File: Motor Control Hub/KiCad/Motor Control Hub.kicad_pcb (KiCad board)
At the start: 2 copper layers, 65 x 41 mm, 8 parts, among them J2 GPIO, J3 Voltage Supply, J4 Motor Controllers

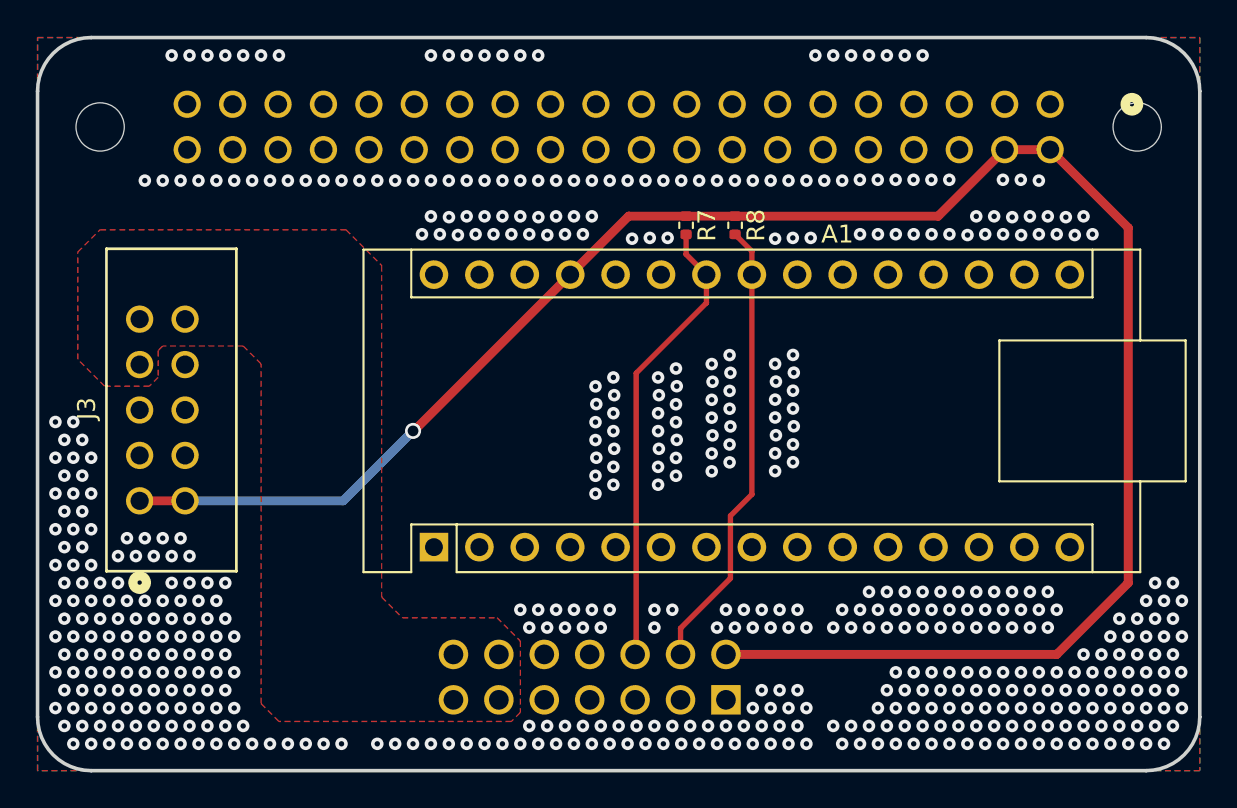
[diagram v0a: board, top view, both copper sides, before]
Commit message: added encoders, slightly adjusted copper tracks
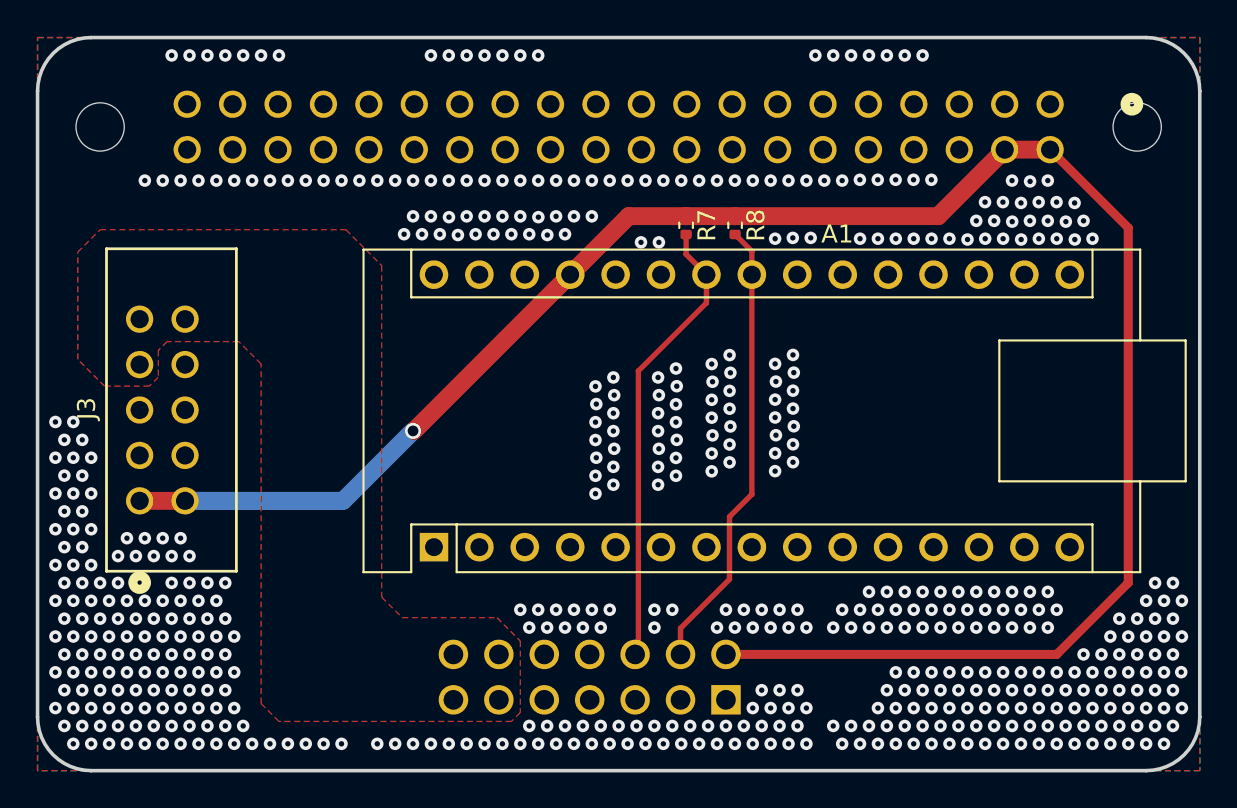
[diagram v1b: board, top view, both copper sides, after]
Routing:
- net GND: vias 533 -> 538
